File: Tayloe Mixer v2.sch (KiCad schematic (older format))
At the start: 38 parts, among them J1 BNC, J2 Pad, J3 Audio_Jack, J4 Conn_01x04_Female, J5 Pad, T1 6:31, T2 31:6, T3 T50_SPLITTER, U1 LM7805_TO220, U2 FST3253, U3 LM358, U4 si5351, U5 LD33V

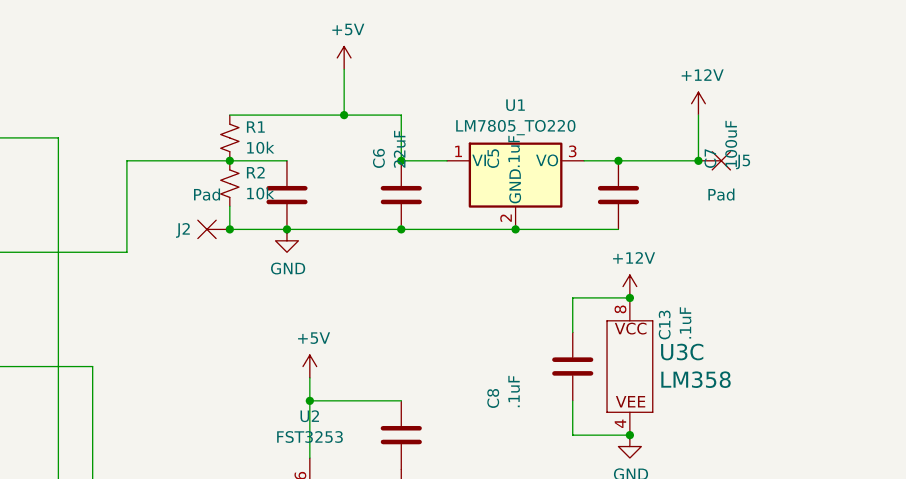
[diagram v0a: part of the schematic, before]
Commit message: swapping caps
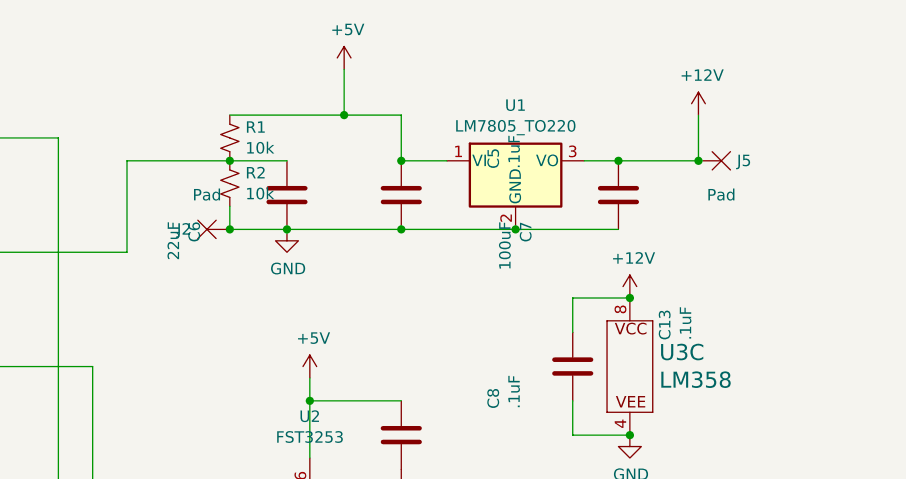
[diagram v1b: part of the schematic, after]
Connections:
- net +12V: now also C7.1; no longer C7.2
- net GND: now also C6.2, C7.2; no longer C6.1, C7.1
- net at R1.2, R2.1, T3.C2A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: now also C6.1; no longer C6.2
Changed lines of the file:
@@
 F 3 "" H 9900 2000 50  0001 C CNN
 	1    9900 2000
-	0    -1   -1   0
+	0    1    1    0
 $EndComp
 $Comp
@@
 F 3 "" H 8450 2000 50  0001 C CNN
 	1    8450 2000
-	0    -1   -1   0
+	0    1    1    0
 $EndComp
 $Comp

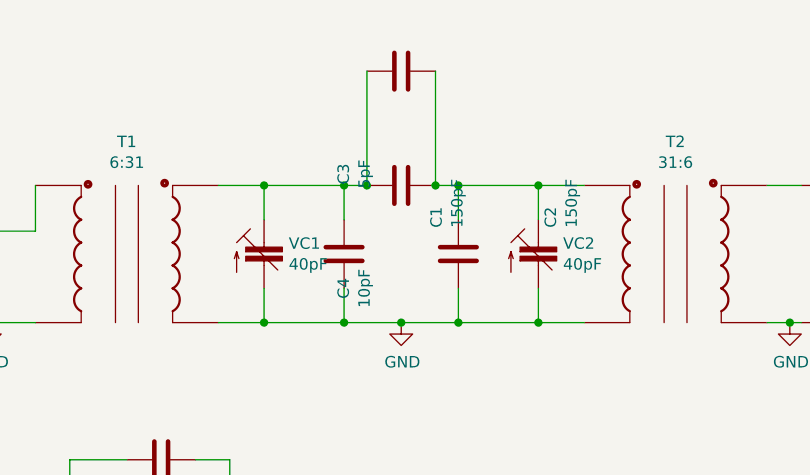
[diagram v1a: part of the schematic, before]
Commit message: Added bands table
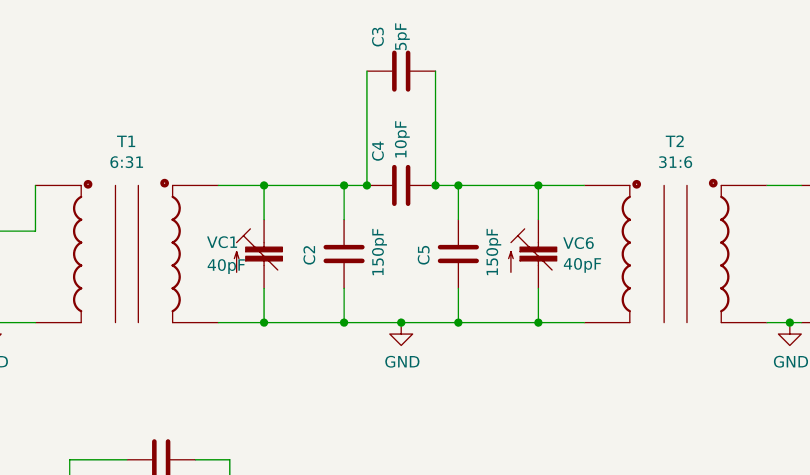
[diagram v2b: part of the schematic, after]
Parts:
- renumbered C1 to C2, C2 to C5, VC2 to VC6

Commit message: gg
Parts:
- renumbered C5 to C25
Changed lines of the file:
@@
 U 1 1 5E9FAC03
 P 8200 1750
-F 0 "R1" H 8268 1796 50  0000 L CNN
-F 1 "10k" H 8268 1705 50  0000 L CNN
+F 0 "R1" H 8050 1800 50  0000 L CNN
+F 1 "10k" H 8050 1700 50  0000 L CNN
 F 2 "Xenir:Capacitor 0805" H 8200 1750 50  0001 C CNN
 F 3 "~" H 8200 1750 50  0001 C CNN
@@
 U 1 1 5E9FB5EE
 P 8200 1950
-F 0 "R2" H 8268 1996 50  0000 L CNN
-F 1 "10k" H 8268 1905 50  0000 L CNN
+F 0 "R2" H 8050 2000 50  0000 L CNN
+F 1 "10k" H 8050 1900 50  0000 L CNN
 F 2 "Xenir:Capacitor 0805" H 8200 1950 50  0001 C CNN
 F 3 "~" H 8200 1950 50  0001 C CNN
@@
 $EndComp
 $Comp
-L Xenir:Capacitor C5
+L Xenir:Capacitor C25
 U 1 1 5E9FBB07
 P 8950 2000
-F 0 "C5" H 9065 1596 50  0000 L CNN
-F 1 ".1uF" H 9065 1505 50  0000 L CNN
+F 0 "C25" H 8900 2150 50  0000 L CNN
+F 1 ".1uF" H 8900 1850 50  0000 L CNN
 F 2 "Xenir:Capacitor 1206" H 8950 2000 50  0001 C CNN
 F 3 "" H 8950 2000 50  0001 C CNN
@@
 U 1 1 5EA05D6A
 P 9900 2000
-F 0 "C7" H 10015 1596 50  0000 L CNN
-F 1 "100uF" H 10015 1505 50  0000 L CNN
+F 0 "C7" H 9850 1850 50  0000 L CNN
+F 1 "100uF" H 9800 2150 50  0000 L CNN
 F 2 "Capacitor_SMD:CP_Elec_6.3x5.4" H 9900 2000 50  0001 C CNN
 F 3 "" H 9900 2000 50  0001 C CNN
@@
 U 1 1 5EA063C0
 P 8450 2000
-F 0 "C6" H 8565 1596 50  0000 L CNN
-F 1 "22uF" H 8565 1505 50  0000 L CNN
+F 0 "C6" H 8450 2150 50  0000 L CNN
+F 1 "22uF" H 8250 2150 50  0000 L CNN
 F 2 "Capacitor_SMD:CP_Elec_4x5.4" H 8450 2000 50  0001 C CNN
 F 3 "" H 8450 2000 50  0001 C CNN
@@
 U 1 1 5EA383DE
 P 8950 3050
-F 0 "C8" H 9065 2646 50  0000 L CNN
-F 1 ".1uF" H 9065 2555 50  0000 L CNN
+F 0 "C8" H 8900 3200 50  0000 L CNN
+F 1 ".1uF" H 8900 2900 50  0000 L CNN
 F 2 "Xenir:Capacitor 1206" H 8950 3050 50  0001 C CNN
 F 3 "" H 8950 3050 50  0001 C CNN
@@
 U 1 1 5EA6792B
 P 4900 3750
-F 0 "C9" H 5015 3346 50  0000 L CNN
-F 1 "470nF" H 5015 3255 50  0000 L CNN
+F 0 "C9" H 4850 3900 50  0000 L CNN
+F 1 "470nF" H 4800 3600 50  0000 L CNN
 F 2 "Xenir:Capacitor 0805" H 4900 3750 50  0001 C CNN
 F 3 "" H 4900 3750 50  0001 C CNN
@@
 U 1 1 5EA68A05
 P 4900 4200
-F 0 "C10" H 5015 3796 50  0000 L CNN
-F 1 "470nF" H 5015 3705 50  0000 L CNN
+F 0 "C10" H 4850 4350 50  0000 L CNN
+F 1 "470nF" H 4800 4050 50  0000 L CNN
 F 2 "Xenir:Capacitor 0805" H 4900 4200 50  0001 C CNN
 F 3 "" H 4900 4200 50  0001 C CNN
@@
 U 1 1 5EA6950B
 P 4900 4700
-F 0 "C11" H 5015 4296 50  0000 L CNN
-F 1 "470nF" H 5015 4205 50  0000 L CNN
+F 0 "C11" H 4850 4850 50  0000 L CNN
+F 1 "470nF" H 4800 4550 50  0000 L CNN
 F 2 "Xenir:Capacitor 0805" H 4900 4700 50  0001 C CNN
 F 3 "" H 4900 4700 50  0001 C CNN
@@
 U 1 1 5EA69901
 P 4900 5150
-F 0 "C12" H 5015 4746 50  0000 L CNN
-F 1 "470nF" H 5015 4655 50  0000 L CNN
+F 0 "C12" H 4850 5300 50  0000 L CNN
+F 1 "470nF" H 4800 5000 50  0000 L CNN
 F 2 "Xenir:Capacitor 0805" H 4900 5150 50  0001 C CNN
 F 3 "" H 4900 5150 50  0001 C CNN
@@
 P 4900 3900
 F 0 "#PWR05" H 4900 3650 50  0001 C CNN
-F 1 "GND" H 4905 3727 50  0000 C CNN
+F 1 "GND" H 5050 3850 50  0000 C CNN
 F 2 "" H 4900 3900 50  0001 C CNN
 F 3 "" H 4900 3900 50  0001 C CNN
@@
 P 4900 4350
 F 0 "#PWR06" H 4900 4100 50  0001 C CNN
-F 1 "GND" H 4905 4177 50  0000 C CNN
+F 1 "GND" H 5050 4300 50  0000 C CNN
 F 2 "" H 4900 4350 50  0001 C CNN
 F 3 "" H 4900 4350 50  0001 C CNN
@@
 P 4900 4850
 F 0 "#PWR07" H 4900 4600 50  0001 C CNN
-F 1 "GND" H 4905 4677 50  0000 C CNN
+F 1 "GND" H 5050 4800 50  0000 C CNN
 F 2 "" H 4900 4850 50  0001 C CNN
 F 3 "" H 4900 4850 50  0001 C CNN
@@
 P 4900 5300
 F 0 "#PWR08" H 4900 5050 50  0001 C CNN
-F 1 "GND" H 4905 5127 50  0000 C CNN
+F 1 "GND" H 5050 5250 50  0000 C CNN
 F 2 "" H 4900 5300 50  0001 C CNN
 F 3 "" H 4900 5300 50  0001 C CNN
@@
 U 1 1 5EA9F5A6
 P 3500 3800
-F 0 "U3" H 3500 4210 70  0000 C CNN
-F 1 "LM358" H 3500 4089 70  0000 C CNN
+F 0 "U3" H 3450 3800 70  0000 C CNN
+F 1 "LM358" H 3750 3650 70  0000 C CNN
 F 2 "Xenir:SOIC8" H 3450 3750 50  0001 C CNN
 F 3 "" H 3450 3750 50  0001 C CNN
@@
 U 2 1 5EAA17EF
 P 3500 4800
-F 0 "U3" H 3500 5210 70  0000 C CNN
-F 1 "LM358" H 3500 5089 70  0000 C CNN
+F 0 "U3" H 3450 4800 70  0000 C CNN
+F 1 "LM358" H 3750 4950 70  0000 C CNN
 F 2 "Xenir:SOIC8" H 3450 4750 50  0001 C CNN
 F 3 "" H 3450 4750 50  0001 C CNN
@@
 U 1 1 5EAC8FB2
 P 9700 2750
-F 0 "C13" H 9815 2346 50  0000 L CNN
-F 1 ".1uF" H 9815 2255 50  0000 L CNN
+F 0 "C13" H 9500 2900 50  0000 L CNN
+F 1 ".1uF" H 9750 2900 50  0000 L CNN
 F 2 "Xenir:Capacitor 1206" H 9700 2750 50  0001 C CNN
 F 3 "" H 9700 2750 50  0001 C CNN
@@
 U 1 1 5EADF0CD
 P 3550 4150
-F 0 "C15" H 3665 3746 50  0000 L CNN
-F 1 "1nF" H 3665 3655 50  0000 L CNN
+F 0 "C15" H 3300 4200 50  0000 L CNN
+F 1 "1nF" H 3650 4200 50  0000 L CNN
 F 2 "Xenir:Capacitor 0805" H 3550 4150 50  0001 C CNN
 F 3 "" H 3550 4150 50  0001 C CNN
@@
 U 1 1 5EADE1CD
 P 3550 3150
-F 0 "C14" H 3665 2746 50  0000 L CNN
-F 1 "1nF" H 3665 2655 50  0000 L CNN
+F 0 "C14" H 3300 3200 50  0000 L CNN
+F 1 "1nF" H 3650 3200 50  0000 L CNN
 F 2 "Xenir:Capacitor 0805" H 3550 3150 50  0001 C CNN
 F 3 "" H 3550 3150 50  0001 C CNN
@@
 P 8100 2000
 F 0 "J2" H 8000 1850 50  0000 C CNN
-F 1 "Pad" H 8100 2000 50  0000 C CNN
+F 1 "Pad" H 8100 1750 50  0000 C CNN
 F 2 "Xenir:Pad" H 8100 2000 50  0001 C CNN
 F 3 "" H 8100 2000 50  0001 C CNN

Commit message: gg
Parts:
- R1, R2, R3, R4, R5, R6, R7, R8: footprint Xenir:Capacitor 0805 -> Xenir:Resistor 0805
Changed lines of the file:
@@
 F 0 "R1" H 8050 1800 50  0000 L CNN
 F 1 "10k" H 8050 1700 50  0000 L CNN
-F 2 "Xenir:Capacitor 0805" H 8200 1750 50  0001 C CNN
+F 2 "Xenir:Resistor 0805" H 8200 1750 50  0001 C CNN
 F 3 "~" H 8200 1750 50  0001 C CNN
 	1    8200 1750
@@
 F 0 "R2" H 8050 2000 50  0000 L CNN
 F 1 "10k" H 8050 1900 50  0000 L CNN
-F 2 "Xenir:Capacitor 0805" H 8200 1950 50  0001 C CNN
+F 2 "Xenir:Resistor 0805" H 8200 1950 50  0001 C CNN
 F 3 "~" H 8200 1950 50  0001 C CNN
 	1    8200 1950
@@
 F 0 "R3" H 4318 3646 50  0000 L CNN
 F 1 "100" H 4318 3555 50  0000 L CNN
-F 2 "Xenir:Capacitor 0805" H 4250 3600 50  0001 C CNN
+F 2 "Xenir:Resistor 0805" H 4250 3600 50  0001 C CNN
 F 3 "~" H 4250 3600 50  0001 C CNN
 	1    4250 3600
@@
 F 0 "R4" H 4318 4096 50  0000 L CNN
 F 1 "100" H 4318 4005 50  0000 L CNN
-F 2 "Xenir:Capacitor 0805" H 4250 4050 50  0001 C CNN
+F 2 "Xenir:Resistor 0805" H 4250 4050 50  0001 C CNN
 F 3 "~" H 4250 4050 50  0001 C CNN
 	1    4250 4050
@@
 F 0 "R5" H 4318 4596 50  0000 L CNN
 F 1 "100" H 4318 4505 50  0000 L CNN
-F 2 "Xenir:Capacitor 0805" H 4250 4550 50  0001 C CNN
+F 2 "Xenir:Resistor 0805" H 4250 4550 50  0001 C CNN
 F 3 "~" H 4250 4550 50  0001 C CNN
 	1    4250 4550
@@
 F 0 "R6" H 4318 5046 50  0000 L CNN
 F 1 "100" H 4318 4955 50  0000 L CNN
-F 2 "Xenir:Capacitor 0805" H 4250 5000 50  0001 C CNN
+F 2 "Xenir:Resistor 0805" H 4250 5000 50  0001 C CNN
 F 3 "~" H 4250 5000 50  0001 C CNN
 	1    4250 5000
@@
 F 0 "R7" H 3618 3346 50  0000 L CNN
 F 1 "10k" H 3618 3255 50  0000 L CNN
-F 2 "Xenir:Capacitor 0805" H 3550 3300 50  0001 C CNN
+F 2 "Xenir:Resistor 0805" H 3550 3300 50  0001 C CNN
 F 3 "~" H 3550 3300 50  0001 C CNN
 	1    3550 3300
@@
 F 0 "R8" H 3618 4346 50  0000 L CNN
 F 1 "10k" H 3618 4255 50  0000 L CNN
-F 2 "Xenir:Capacitor 0805" H 3550 4300 50  0001 C CNN
+F 2 "Xenir:Resistor 0805" H 3550 4300 50  0001 C CNN
 F 3 "~" H 3550 4300 50  0001 C CNN
 	1    3550 4300

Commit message: rescue
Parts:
- C10, C11, C12, C13, C14, C15, C2, C25, C3, C4, C5, C6, C7, C8, C9: symbol Xenir:Capacitor -> Tayloe-Mixer-v2-rescue:Capacitor-Xenir
- J1: symbol Xenir:BNC -> Tayloe-Mixer-v2-rescue:BNC-Xenir
- J2, J5: symbol Xenir:Pad -> Tayloe-Mixer-v2-rescue:Pad-Xenir
- J3: symbol Xenir:Audio_Jack -> Tayloe-Mixer-v2-rescue:Audio_Jack-Xenir
- T1, T2: symbol Xenir:T37_XFRM -> Tayloe-Mixer-v2-rescue:T37_XFRM-Xenir
- T3: symbol Xenir:T50_SPLITTER -> Tayloe-Mixer-v2-rescue:T50_SPLITTER-Xenir
- U2: symbol Xenir:FST3253 -> Tayloe-Mixer-v2-rescue:FST3253-Xenir
- U3: symbol Xenir:LM358 -> Tayloe-Mixer-v2-rescue:LM358-Xenir
- U4: symbol Xenir:si5351 -> Tayloe-Mixer-v2-rescue:si5351-Xenir
- U5: symbol Xenir:LD33V -> Tayloe-Mixer-v2-rescue:LD33V-Xenir
- VC1, VC6: symbol Xenir:Trimcap -> Tayloe-Mixer-v2-rescue:Trimcap-Xenir
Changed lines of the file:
@@
 $EndComp
 $Comp
-L Xenir:Capacitor C25
+L Tayloe-Mixer-v2-rescue:Capacitor-Xenir C25
 U 1 1 5E9FBB07
 P 8950 2000
@@
 	7750 1850 8200 1850
 $Comp
-L Xenir:Capacitor C7
+L Tayloe-Mixer-v2-rescue:Capacitor-Xenir C7
 U 1 1 5EA05D6A
 P 9900 2000
@@
 $EndComp
 $Comp
-L Xenir:Capacitor C6
+L Tayloe-Mixer-v2-rescue:Capacitor-Xenir C6
 U 1 1 5EA063C0
 P 8450 2000
@@
 	8700 1650 8950 1650
 $Comp
-L Xenir:FST3253 U2
+L Tayloe-Mixer-v2-rescue:FST3253-Xenir U2
 U 1 1 5EA318D2
 P 9000 2700
@@
 	8550 2800 8550 2900
 $Comp
-L Xenir:Capacitor C8
+L Tayloe-Mixer-v2-rescue:Capacitor-Xenir C8
 U 1 1 5EA383DE
 P 8950 3050
@@
 	9550 4250 9250 4250
 $Comp
-L Xenir:Capacitor C9
+L Tayloe-Mixer-v2-rescue:Capacitor-Xenir C9
 U 1 1 5EA6792B
 P 4900 3750
@@
 $EndComp
 $Comp
-L Xenir:Capacitor C10
+L Tayloe-Mixer-v2-rescue:Capacitor-Xenir C10
 U 1 1 5EA68A05
 P 4900 4200
@@
 $EndComp
 $Comp
-L Xenir:Capacitor C11
+L Tayloe-Mixer-v2-rescue:Capacitor-Xenir C11
 U 1 1 5EA6950B
 P 4900 4700
@@
 $EndComp
 $Comp
-L Xenir:Capacitor C12
+L Tayloe-Mixer-v2-rescue:Capacitor-Xenir C12
 U 1 1 5EA69901
 P 4900 5150
@@
 $EndComp
 $Comp
-L Xenir:LM358 U3
+L Tayloe-Mixer-v2-rescue:LM358-Xenir U3
 U 1 1 5EA9F5A6
 P 3500 3800
@@
 $EndComp
 $Comp
-L Xenir:LM358 U3
+L Tayloe-Mixer-v2-rescue:LM358-Xenir U3
 U 2 1 5EAA17EF
 P 3500 4800
@@
 $EndComp
 $Comp
-L Xenir:LM358 U3
+L Tayloe-Mixer-v2-rescue:LM358-Xenir U3
 U 3 1 5EAA2951
 P 10050 2750
@@
 $EndComp
 $Comp
-L Xenir:Capacitor C13
+L Tayloe-Mixer-v2-rescue:Capacitor-Xenir C13
 U 1 1 5EAC8FB2
 P 9700 2750
@@
 $EndComp
 $Comp
-L Xenir:Capacitor C15
+L Tayloe-Mixer-v2-rescue:Capacitor-Xenir C15
 U 1 1 5EADF0CD
 P 3550 4150
@@
 	3850 4300 3850 4700
 $Comp
-L Xenir:Capacitor C14
+L Tayloe-Mixer-v2-rescue:Capacitor-Xenir C14
 U 1 1 5EADE1CD
 P 3550 3150
@@
 	6200 1950 6350 1950
 $Comp
-L Xenir:T50_SPLITTER T3
+L Tayloe-Mixer-v2-rescue:T50_SPLITTER-Xenir T3
 U 1 1 5E9EEE06
 P 6700 1550
@@
 	4750 1950 4850 1950
 $Comp
-L Xenir:T37_XFRM T2
+L Tayloe-Mixer-v2-rescue:T37_XFRM-Xenir T2
 U 1 1 5E9E9ADC
 P 5800 1800
@@
 $EndComp
 $Comp
-L Xenir:Trimcap VC6
+L Tayloe-Mixer-v2-rescue:Trimcap-Xenir VC6
 U 1 1 5E9E8F97
 P 5200 1850
@@
 $EndComp
 $Comp
-L Xenir:Capacitor C3
+L Tayloe-Mixer-v2-rescue:Capacitor-Xenir C3
 U 1 1 5E9E8D24
 P 4600 1450
@@
 $EndComp
 $Comp
-L Xenir:Capacitor C4
+L Tayloe-Mixer-v2-rescue:Capacitor-Xenir C4
 U 1 1 5E9E81AF
 P 4600 1950
@@
 $EndComp
 $Comp
-L Xenir:Capacitor C5
+L Tayloe-Mixer-v2-rescue:Capacitor-Xenir C5
 U 1 1 5E9E7736
 P 4850 2250
@@
 $EndComp
 $Comp
-L Xenir:Capacitor C2
+L Tayloe-Mixer-v2-rescue:Capacitor-Xenir C2
 U 1 1 5E9E667F
 P 4350 2250
@@
 $EndComp
 $Comp
-L Xenir:Trimcap VC1
+L Tayloe-Mixer-v2-rescue:Trimcap-Xenir VC1
 U 1 1 5E9DC9D6
 P 4000 1850
@@
 	3000 2150 3000 1950
 $Comp
-L Xenir:T37_XFRM T1
+L Tayloe-Mixer-v2-rescue:T37_XFRM-Xenir T1
 U 1 1 5E9D7159
 P 3400 1800
@@
 Connection ~ 3150 4800
 $Comp
-L Xenir:si5351 U4
+L Tayloe-Mixer-v2-rescue:si5351-Xenir U4
 U 1 1 5E9EA10D
 P 11600 3250
@@
 $EndComp
 $Comp
-L Xenir:Audio_Jack J3
+L Tayloe-Mixer-v2-rescue:Audio_Jack-Xenir J3
 U 1 1 5E9E7BEE
 P 2250 4600
@@
 	10000 3750 9250 3750
 $Comp
-L Xenir:BNC J1
+L Tayloe-Mixer-v2-rescue:BNC-Xenir J1
 U 1 1 5F44E5DC
 P 2100 2150
@@
 $EndComp
 $Comp
-L Xenir:LD33V U5
+L Tayloe-Mixer-v2-rescue:LD33V-Xenir U5
 U 1 1 5F4A2EFF
 P 11850 1700
@@
 Connection ~ 2450 4350
 $Comp
-L Xenir:Pad J5
+L Tayloe-Mixer-v2-rescue:Pad-Xenir J5
 U 1 1 5F486548
 P 10350 2000
@@
 Connection ~ 10250 1850
 $Comp
-L Xenir:Pad J2
+L Tayloe-Mixer-v2-rescue:Pad-Xenir J2
 U 1 1 5F4876B8
 P 8100 2000
